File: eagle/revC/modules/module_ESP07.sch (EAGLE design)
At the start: 27 parts

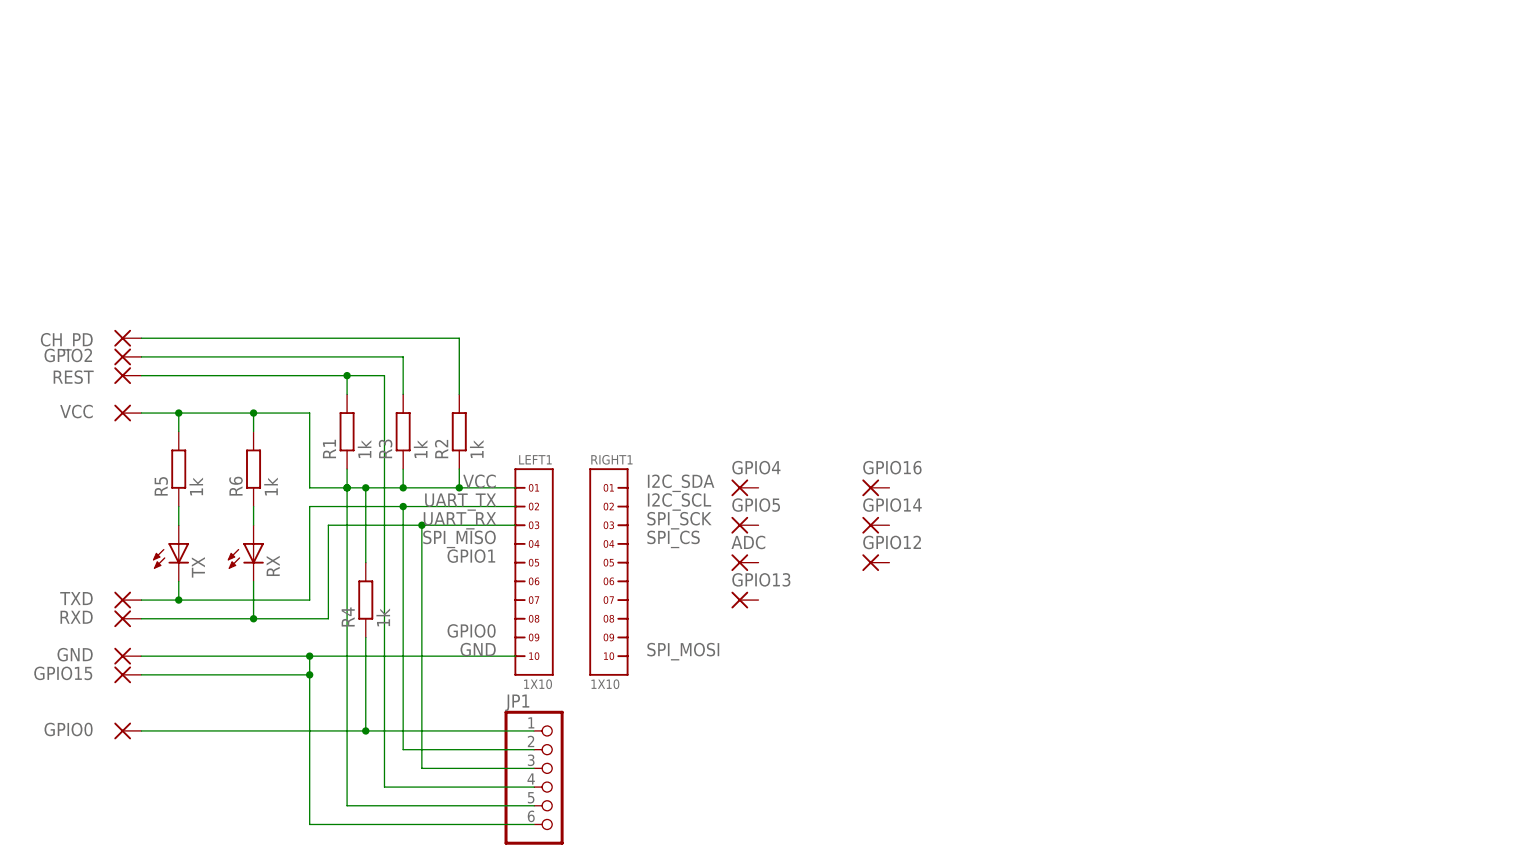
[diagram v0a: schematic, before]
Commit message: Replaced modules with library parts
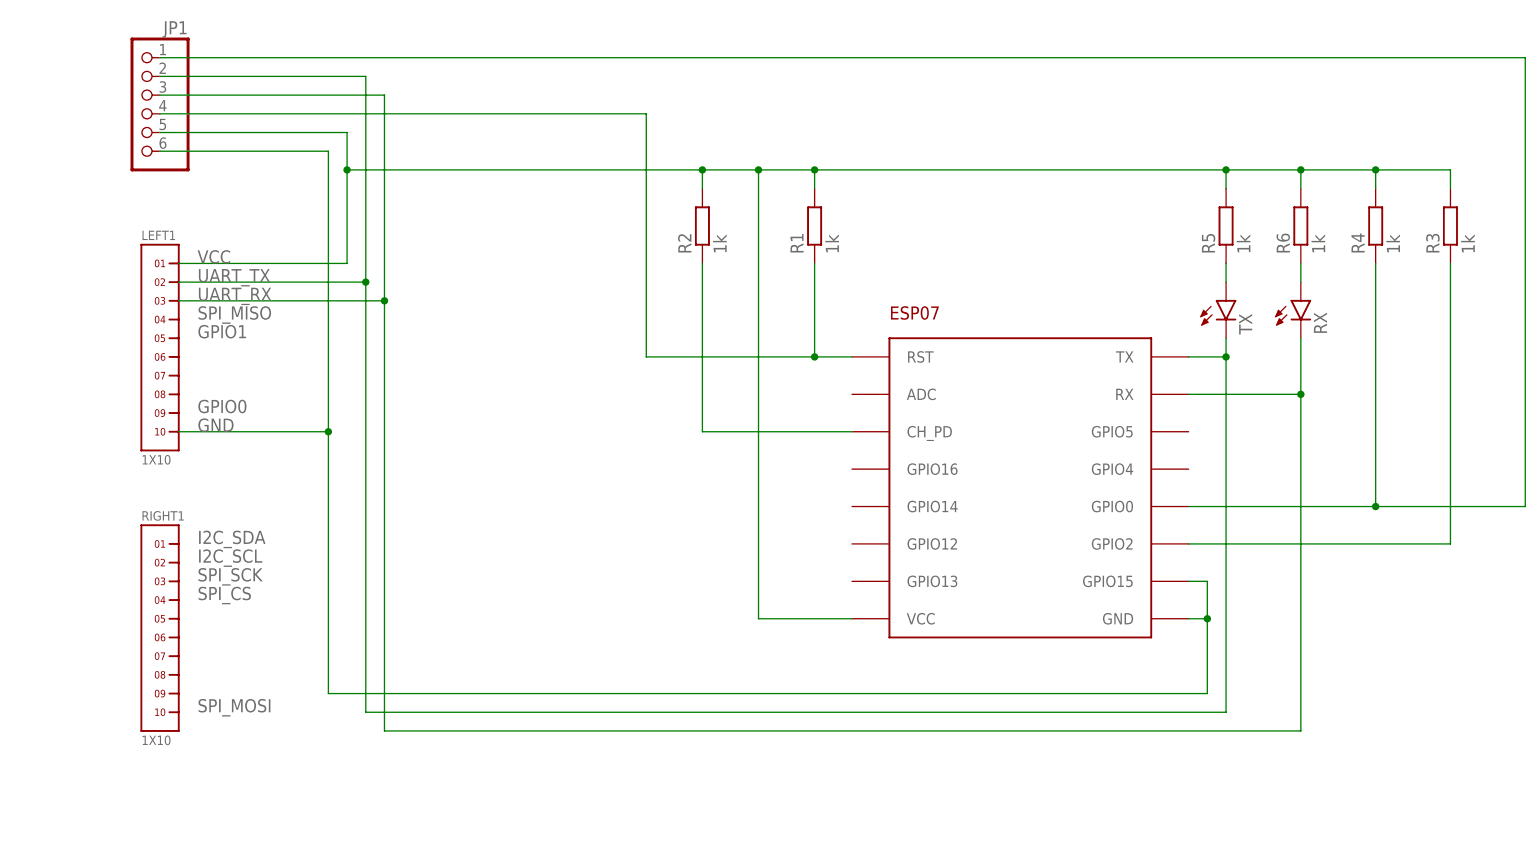
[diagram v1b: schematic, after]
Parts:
- removed ADC, CH_PD, GND, GPIO0, GPIO12, GPIO13, GPIO14, GPIO15, GPIO16, GPIO2, GPIO4, GPIO5, REST, RXD, TXD, VCC: WIREPADSMD1,27-254, wirepad:WIREPADSMD1,27-254
- added U$1: ESP-07, RadioShield:ESP-07
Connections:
- removed net N$1: GPIO2.P, R3.2
- removed net N$2: CH_PD.P, R2.2
- new net N$6: R2.1, U$1.CH_PD
- new net N$7: R3.1, U$1.GPIO2
- net GND: now also U$1.GND, U$1.GPIO15; no longer GND.P, GPIO15.P
- net GPIO0: now also U$1.GPIO0; no longer GPIO0.P
- net RST: now also R1.1, U$1.RST; no longer R1.2, REST.P
- net UART_RX: now also U$1.RX; no longer RXD.P
- net UART_TX: now also U$1.TX; no longer TXD.P
- net VCC: now also R1.2, R2.2, R3.2, U$1.VCC; no longer R1.1, R2.1, R3.1, VCC.P
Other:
- moved on the sheet: JP1, LEFT1, R1, R2, R3, R4, R5, R6, RIGHT1
